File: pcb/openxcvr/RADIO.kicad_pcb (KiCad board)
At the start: 2 copper layers, 99.1 x 63.5 mm, 118 parts, among them J1 UI_CONNECTOR, J2 GPS_CONNECTOR, J3 PA_CONNECTOR, U1 PCM1802, U10 MAX_1000, U11 24LC256, U2 LM386, U3 MCP6002-xSN, U4 FST5253, U5 LM4562, U6 LM4562, U7 LM4562, U8 FST5253, U9 FST5253

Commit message: Get things working with rev 1 PCB
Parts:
- removed C25, C26, C27: 1u, Capacitor_SMD:C_0805_2012Metric
- removed R16, R17: 150, Resistor_SMD:R_0805_2012Metric
- removed R19, R20, R21, R23, R24, R25, R26, R27, R28, R29: 2K2, Resistor_SMD:R_0805_2012Metric
- removed U6, U7: LM4562, Package_SO:SOIC-8_3.9x4.9mm_P1.27mm
- added T1: cx2074NL, openxcvr:bn43-2402-transformer, F.Cu at (122.6, 62.9)
- C20, C21: value 100n -> 22n
- C22, C23: value 100n -> 390p
- C24: value 1u -> 100n
- R12: value 10K -> 1K
- R13: value 10K -> 82
- R14, R15: value 10K -> 100
- U8, U9: value FST5253 -> 74LS251
- moved C24 59.7 mm to (168.2, 98.3)
- moved C31 40.9 mm to (97.8, 63.5)
- moved U11 39.9 mm to (120.7, 95.2)
- moved R30 37.6 mm to (100.3, 58.3), turned to 0 degrees
- moved C23 34.4 mm to (144.8, 78.1)
- moved C36 33.4 mm to (99.1, 97.2), turned to 0 degrees
- moved C49 32.7 mm to (110.5, 69.2), turned to 180 degrees
- moved R12 31.8 mm to (138.4, 83.8), turned to 0 degrees
- moved C32 31.1 mm to (97.8, 102.9)
- moved C21 30.7 mm to (144.8, 70.5), turned to 0 degrees
- moved C40 30.4 mm to (99.1, 94.6), turned to 0 degrees
- moved C45 29.4 mm to (110.5, 71.8), turned to 0 degrees
- moved L5 29.1 mm to (110.5, 76.2), turned to 90 degrees
- moved R15 27.1 mm to (144.8, 73.0)
- moved U9 26.7 mm to (104.1, 63.5), turned to 90 degrees
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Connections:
- C20 pad 1: +2V5 -> GND
- C20 pad 2: I_NEG -> Net-(C20-Pad2)
- C21 pad 1: +2V5 -> GND
- C21 pad 2: Q_NEG -> Net-(C21-Pad2)
- C22 pad 1: I_POS -> Net-(C22-Pad1)
- C22 pad 2: +2V5 -> Net-(C22-Pad2)
- C23 pad 1: Q_POS -> Net-(C23-Pad1)
- C23 pad 2: +2V5 -> Net-(C23-Pad2)
- C24 pad 1: I_POS -> SPEAKER
- C28 pad 1: Net-(C28-Pad1) -> Net-(C22-Pad2)
- C29 pad 1: Net-(C29-Pad1) -> Net-(C23-Pad2)
- R11 pad 1: RF_BPF -> Net-(R11-Pad1)
- R12 pad 1: Net-(C24-Pad2) -> +5V
- R12 pad 2: +2V5 -> Net-(C5-Pad1)
- R13 pad 1: +2V5 -> Net-(R13-Pad1)
- R13 pad 2: Net-(C25-Pad2) -> Net-(R13-Pad2)
- R14 pad 1: Net-(C26-Pad2) -> Net-(C22-Pad1)
- R14 pad 2: +2V5 -> Net-(C20-Pad2)
- R15 pad 1: +2V5 -> Net-(C23-Pad1)
- R15 pad 2: Net-(C27-Pad2) -> Net-(C21-Pad2)
- R18 pad 1: Net-(R16-Pad2) -> Net-(C22-Pad1)
- R18 pad 2: Net-(R18-Pad2) -> Net-(C22-Pad2)
- R2 pad 1: SPEAKER -> Net-(C24-Pad2)
- R22 pad 1: Net-(R18-Pad2) -> Net-(C23-Pad1)
- R22 pad 2: Net-(R22-Pad2) -> Net-(C23-Pad2)
- U4 pad 10: I_POS -> Net-(C21-Pad2)
- U4 pad 11: Q_POS -> Net-(U4-Pad11)
- U4 pad 12: Q_NEG -> Net-(C20-Pad2)
- U4 pad 13: I_NEG -> Net-(U4-Pad13)
- U4 pad 3: I_NEG -> Net-(C21-Pad2)
- U4 pad 4: Q_NEG -> Net-(U4-Pad4)
- U4 pad 5: Q_POS -> Net-(C20-Pad2)
- U4 pad 6: I_POS -> Net-(U4-Pad6)
- U4 pad 9: Net-(R11-Pad2) -> Net-(R13-Pad2)
- U5 pad 1: Net-(R19-Pad2) -> Net-(C23-Pad2)
- U5 pad 2: Net-(R16-Pad1) -> Net-(C23-Pad1)
- U5 pad 3: Net-(C25-Pad2) -> +2V5
- U5 pad 5: Net-(C24-Pad2) -> +2V5
- U5 pad 6: Net-(R16-Pad2) -> Net-(C22-Pad1)
- U5 pad 7: Net-(R18-Pad2) -> Net-(C22-Pad2)
- U8 pad 1: GND -> BPF_2_4_A
- U8 pad 10: BPF_16_30_B -> BAND_1
- U8 pad 11: BPF_8_16_B -> BAND_0
- U8 pad 12: BPF_4_8_B -> Net-(U8-Pad12)
- U8 pad 13: BPF_2_4_B -> Net-(U8-Pad12)
- U8 pad 14: BAND_0 -> Net-(U8-Pad12)
- U8 pad 15: GND -> Net-(U8-Pad12)
- U8 pad 2: BAND_1 -> BPF_4_8_A
- U8 pad 3: BPF_2_4_A -> BPF_8_16_A
- U8 pad 4: BPF_4_8_A -> BPF_16_30_A
- U8 pad 5: BPF_8_16_A -> Net-(C30-Pad2)
- U8 pad 6: BPF_16_30_A -> Net-(U8-Pad6)
- U8 pad 7: BANK_0_A -> GND
- U8 pad 9: BANK_0_B -> BAND_2
- U9 pad 1: GND -> BPF_2_4_B
- U9 pad 10: BANK_0_B -> BAND_1
- U9 pad 11: Net-(U9-Pad11) -> BAND_0
- U9 pad 12: Net-(U9-Pad12) -> Net-(U8-Pad12)
- U9 pad 13: Net-(U9-Pad13) -> Net-(U8-Pad12)
- U9 pad 14: BAND_2 -> Net-(U8-Pad12)
- U9 pad 15: GND -> Net-(U8-Pad12)
- U9 pad 2: GND -> BPF_4_8_B
- U9 pad 3: Net-(U9-Pad3) -> BPF_8_16_B
- U9 pad 4: Net-(U9-Pad4) -> BPF_16_30_B
- U9 pad 5: Net-(U9-Pad11) -> RF_BPF
- U9 pad 6: BANK_0_A -> Net-(U9-Pad6)
- U9 pad 7: Net-(C30-Pad2) -> GND
- U9 pad 9: RF_BPF -> BAND_2
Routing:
- net +5V: track 205.3 -> 283.1 mm, vias 16 -> 8
- net Net-(U8-Pad12): track 0.00 -> 75.6 mm
- net BAND_0: track 27.8 -> 91.5 mm, vias 2 -> 1
- net BAND_1: track 33.5 -> 91.7 mm, vias 2 -> 1
- net GND: track 99.3 -> 44.6 mm, vias 23 -> 58
- net BPF_2_4_B: track 55.9 -> 3.70 mm
- net Net-(C13-Pad1): track 98.1 -> 47.5 mm, vias 0 -> 2
- net Net-(C24-Pad2): track 50.1 -> 3.42 mm
- net BPF_4_8_B: track 46.6 -> 3.64 mm
- net Net-(C26-Pad2): track 42.2 -> 0.00 mm
- net Net-(U10-Pad20): track 45.6 -> 5.41 mm, vias 2 -> 0
- net BAND_2: track 28.0 -> 64.3 mm, vias 2 -> 1
- net +2V5: track 147.6 -> 183.8 mm, vias 8 -> 2
- net I_POS: track 35.2 -> 0.00 mm
- net LCD_CONTRAST: track 36.0 -> 70.8 mm
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
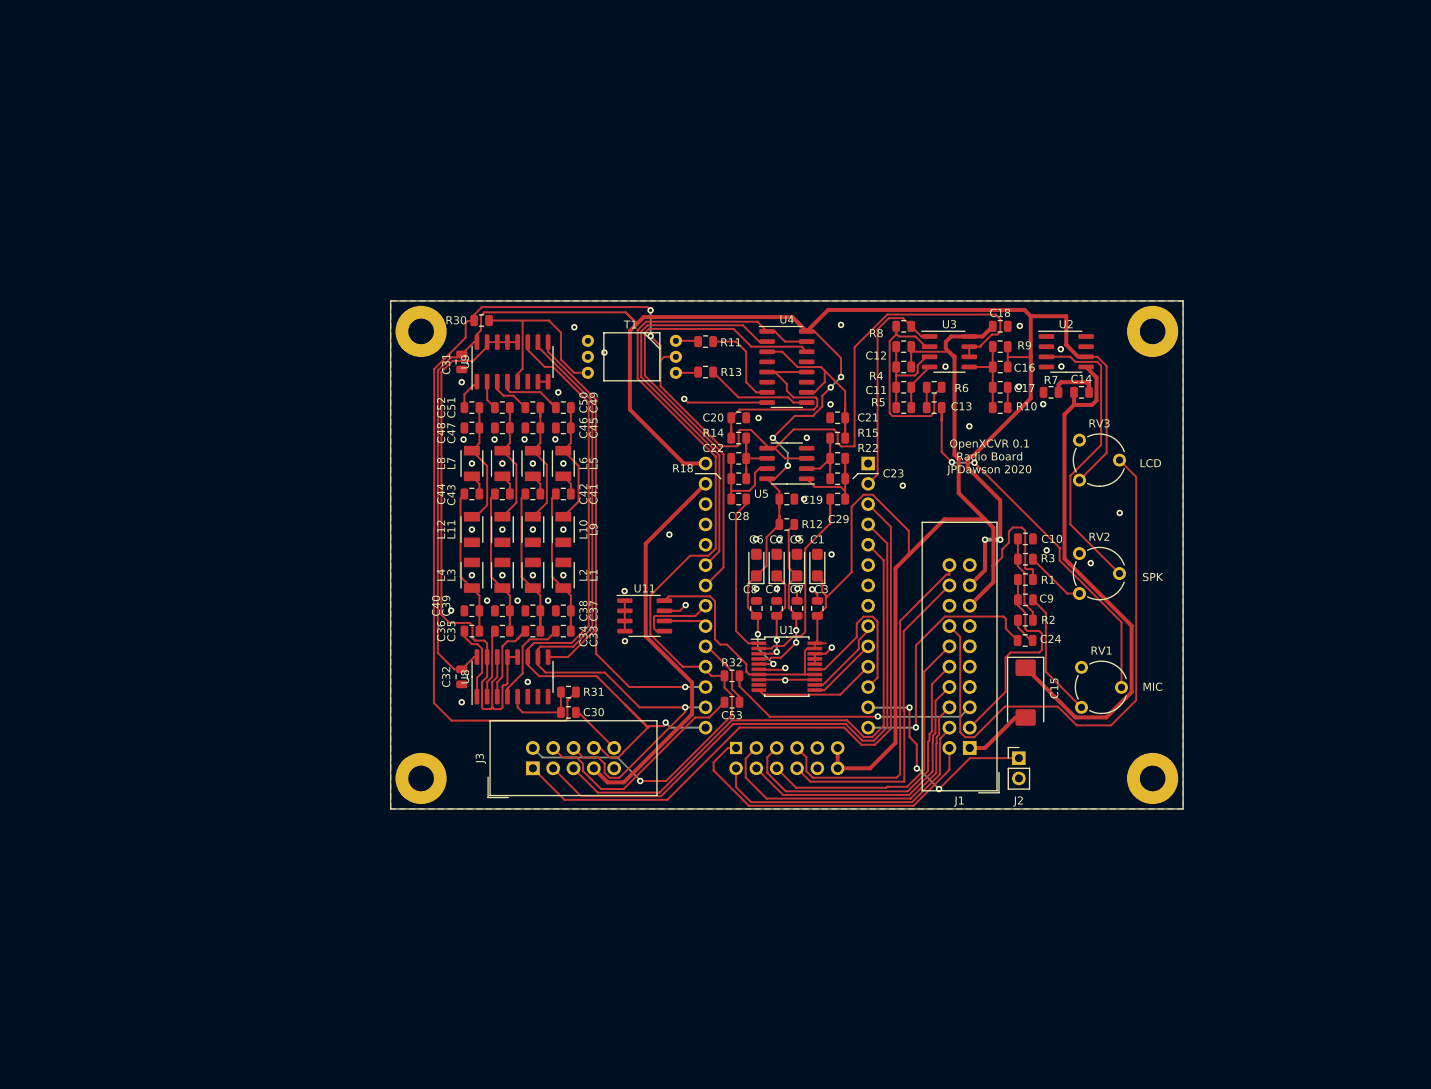
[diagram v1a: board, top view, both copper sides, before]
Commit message: Add eeprom load store capability
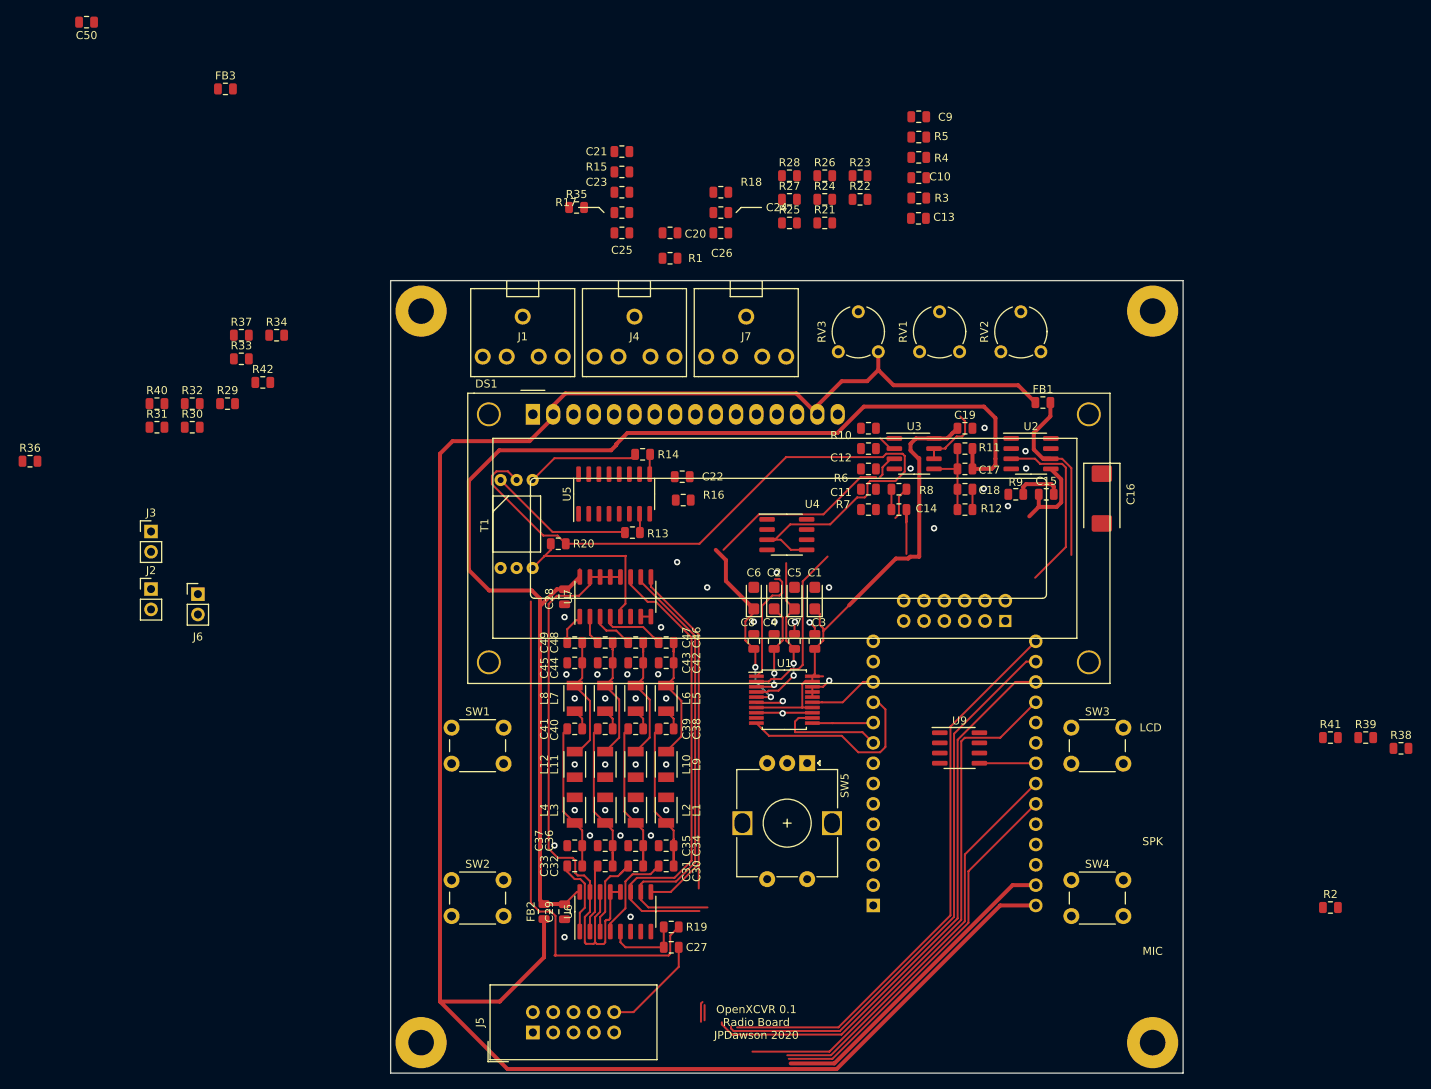
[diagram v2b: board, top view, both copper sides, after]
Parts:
- added DS1: WC1602A, Display:WC1602A, F.Cu at (106.7, 70.1)
- added FB1: Ferrite_Bead, Inductor_SMD:L_0805_2012Metric, F.Cu at (170.4, 68.6)
- added FB2: Ferrite_Bead, Inductor_SMD:L_0805_2012Metric, F.Cu at (108.1, 132.2)
- added FB3: Ferrite_Bead, Inductor_SMD:L_0805_2012Metric, F.Cu at (68.3, 29.4)
- added J2: Mic, Connector_PinHeader_2.54mm:PinHeader_1x02_P2.54mm_Vertical, F.Cu at (59.0, 91.9)
- added J3: Speaker, Connector_PinHeader_2.54mm:PinHeader_1x02_P2.54mm_Vertical, F.Cu at (59.0, 84.7)
- added J4: Headphone, openxcvr:jack3.5mm switched, F.Cu at (119.4, 53.3)
- added J7: PTT, openxcvr:jack3.5mm switched, F.Cu at (133.3, 53.3)
- added R2: 1K, Resistor_SMD:R_0805_2012Metric, F.Cu at (206.4, 131.7)
- added R21: 100, Resistor_SMD:R_0805_2012Metric, F.Cu at (143.2, 46.1)
- added R22: 100, Resistor_SMD:R_0805_2012Metric, F.Cu at (147.6, 43.2)
- added R23: 100, Resistor_SMD:R_0805_2012Metric, F.Cu at (147.6, 40.2)
- added R24: 100, Resistor_SMD:R_0805_2012Metric, F.Cu at (143.2, 43.2)
- added R25: 100, Resistor_SMD:R_0805_2012Metric, F.Cu at (138.8, 46.1)
- added R26: 100, Resistor_SMD:R_0805_2012Metric, F.Cu at (143.2, 40.2)
- added R27: 100, Resistor_SMD:R_0805_2012Metric, F.Cu at (138.8, 43.2)
- added R28: 100, Resistor_SMD:R_0805_2012Metric, F.Cu at (138.8, 40.2)
- added R29: 10K, Resistor_SMD:R_0805_2012Metric, F.Cu at (68.5, 68.7)
- added R30: 10K, Resistor_SMD:R_0805_2012Metric, F.Cu at (64.1, 71.7)
- added R31: 10K, Resistor_SMD:R_0805_2012Metric, F.Cu at (59.7, 71.7)
- added R33: 10K, Resistor_SMD:R_0805_2012Metric, F.Cu at (70.2, 63.1)
- added R34: 2K2, Resistor_SMD:R_0805_2012Metric, F.Cu at (74.7, 60.2)
- added R35: 2K2, Resistor_SMD:R_0805_2012Metric, F.Cu at (112.1, 44.2)
- added R36: 2K2, Resistor_SMD:R_0805_2012Metric, F.Cu at (43.8, 75.9)
- added R37: 2K2, Resistor_SMD:R_0805_2012Metric, F.Cu at (70.2, 60.2)
- added R38: 2K2, Resistor_SMD:R_0805_2012Metric, F.Cu at (215.2, 111.8)
- added R39: 2K2, Resistor_SMD:R_0805_2012Metric, F.Cu at (210.8, 110.5)
- added R40: 10K, Resistor_SMD:R_0805_2012Metric, F.Cu at (59.7, 68.7)
- added R41: 2K2, Resistor_SMD:R_0805_2012Metric, F.Cu at (206.4, 110.5)
- added R42: 10K, Resistor_SMD:R_0805_2012Metric, F.Cu at (72.9, 66.1)
- added SW1: SW_Push, Button_Switch_THT:SW_PUSH_6mm, F.Cu at (96.5, 109.2)
- added SW2: SW_Push, Button_Switch_THT:SW_PUSH_6mm, F.Cu at (96.5, 128.3)
- added SW3: SW_Push, Button_Switch_THT:SW_PUSH_6mm, F.Cu at (174.0, 109.2)
- added SW4: SW_Push, Button_Switch_THT:SW_PUSH_6mm, F.Cu at (174.0, 128.3)
- added SW5: Rotary_Encoder_Switch, Rotary_Encoder:RotaryEncoder_Alps_EC12E-Switch_Vertical_H20mm, F.Cu at (141.0, 113.7)
- C23: renamed from C22; value 390p -> 1n
- C24: renamed from C23; value 390p -> 1n
- J1: value UI_CONNECTOR -> Microphone; footprint Connector_IDC:IDC-Header_2x10_P2.54mm_Vertical -> openxcvr:jack3.5mm switched
- T1: value cx2074NL -> BN43-24023
- moved C50 117.2 mm to (50.9, 21.0)
- moved J6 104.7 mm to (64.8, 92.5)
- moved U8 103.1 mm to (159.4, 154.3), turned to 0 degrees
- moved J1 80.8 mm to (105.4, 53.3), turned to 0 degrees
- moved R32 75.6 mm to (64.1, 68.7)
- moved C13 54.4 mm to (154.9, 45.6)
- moved R5 54.4 mm to (154.9, 35.4)
- moved C10 54.4 mm to (154.9, 40.5)
- moved C9 54.4 mm to (154.9, 32.9)
- moved R4 54.4 mm to (154.9, 37.9)
- moved R3 54.4 mm to (154.9, 43.0)
- moved RV2 44.7 mm to (170.2, 62.2), turned to 90 degrees
- moved U9 42.7 mm to (160.0, 111.8)
- moved R15 36.3 mm to (117.8, 39.8)
- moved C21 36.3 mm to (117.8, 37.2)
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- renumbered C9 to C10, C24 to C13, C13 to C14, C14 to C15, C15 to C16, C16 to C17, C17 to C18, C18 to C19, C19 to C20, C20 to C21, C21 to C22, C28 to C25, C29 to C26, C30 to C27, C31 to C28, C32 to C29, C33 to C30, C34 to C31, C35 to C32, C36 to C33, C37 to C34, C38 to C35, C39 to C36, C40 to C37, C41 to C38, C42 to C39, C43 to C40, C44 to C41, C45 to C42, C46 to C43, C47 to C44, C48 to C45, C49 to C46, C50 to C47, C51 to C48, C52 to C49, C53 to C50, C10 to C9, J3 to J5, J2 to J6, R12 to R1, R8 to R10, R9 to R11, R10 to R12, R11 to R13, R13 to R14, R14 to R15, R15 to R16, R18 to R17, R22 to R18, R31 to R19, R30 to R20, R2 to R3, R1 to R4, R3 to R5, R4 to R6, R5 to R7, R6 to R8, R7 to R9, RV2 to RV1, RV1 to RV2, U5 to U4, U4 to U5, U8 to U6, U9 to U7, U10 to U8, U11 to U9
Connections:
- C10 pad 1: MIC_HDR -> Net-(C10-Pad1)
- C13 pad 1: SPEAKER -> Net-(C13-Pad1)
- C13 pad 2: Net-(C24-Pad2) (its old number) -> Net-(C13-Pad2)
- C16 pad 2: SPEAKER_HDR -> Net-(C16-Pad2)
- C21 pad 2: Net-(C20-Pad2) -> Net-(C21-Pad2)
- R15 pad 2: Net-(C20-Pad2) -> Net-(C21-Pad2)
- R3 pad 1: Net-(C24-Pad2) (its old number) -> SPEAKER
- R32 pad 1: TX_ENABLE -> LCD7
- R32 pad 2: Net-(J1-Pad5) -> Net-(R32-Pad2)
- R4 pad 2: MIC_HDR -> Net-(C10-Pad1)
- RV1 pad 2: Net-(RV2-Pad2) -> Net-(C13-Pad1)
- RV3 pad 1: +5V -> +5VD
- RV3 pad 2: LCD_CONTRAST -> Net-(DS1-Pad3)
- U2 pad 3: Net-(RV2-Pad2) -> Net-(C13-Pad2)
- U2 pad 6: +5V -> +5VA
- U5 pad 12: Net-(C20-Pad2) -> Net-(U5-Pad12)
- U5 pad 13: Net-(U4-Pad13) -> Net-(C21-Pad2)
- U5 pad 5: Net-(C20-Pad2) -> Net-(U5-Pad5)
- U5 pad 6: Net-(U4-Pad6) -> Net-(C21-Pad2)
- U8 pad 28: +5V -> +5VD
- U8 pad 29: LCD7 -> Net-(R21-Pad2)
- U8 pad 30: LCD5 -> Net-(R22-Pad2)
- U8 pad 31: LCD_RS -> Net-(R23-Pad2)
- U8 pad 32: PB_1 -> Net-(R24-Pad2)
- U8 pad 34: +3V3 -> Net-(FB3-Pad1)
- U8 pad 35: LCD6 -> Net-(R25-Pad1)
- U8 pad 36: LCD4 -> Net-(R26-Pad1)
- U8 pad 37: LCD_E -> Net-(R27-Pad1)
- U8 pad 38: PB_0 -> Net-(R28-Pad1)
- U8 pad 40: +3V3 -> Net-(FB3-Pad1)
- U8 pad 6: Net-(U10-Pad6) -> PTT
- U8 pad 7: Net-(U10-Pad7) -> DIT
- U8 pad 8: Net-(U10-Pad8) -> DAH
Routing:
- net +5VD: track 0.00 -> 261.4 mm
- net +3V3: track 181.7 -> 60.6 mm
- net BATTERY: track 81.1 -> 0.00 mm
- net +5V: track 283.1 -> 202.1 mm, vias 8 -> 2
- net FWD_PWR: track 74.9 -> 0.00 mm
- net LCD_CONTRAST: track 70.8 -> 0.00 mm
- net REV_PWR: track 68.7 -> 0.00 mm
- net BAND_2: track 64.3 -> 120.2 mm, vias 1 -> 0
- net Net-(C15-Pad1): track 66.3 -> 11.0 mm
- net TX_ENABLE: track 116.6 -> 66.6 mm, vias 1 -> 0
- net PB_1: track 44.5 -> 0.00 mm
- net PB_0: track 41.0 -> 0.00 mm
- net LCD7: track 40.5 -> 0.00 mm
- net Net-(C14-Pad1): track 47.5 -> 7.17 mm, vias 2 -> 0
- net LCD_RS: track 39.9 -> 0.00 mm
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- removed copper zone on B.Cu, net GND
- removed copper zone on F.Cu, net GND
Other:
- board size 99.1 x 63.5 mm -> 99.1 x 99.1 mm

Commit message: update rev0.2 PCB
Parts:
- removed C16: 100u, Capacitor_Tantalum_SMD:CP_EIA-7343-31_Kemet-D
- removed C50: 100n, Capacitor_SMD:C_0805_2012Metric
- removed RV1, RV2: 10K, Potentiometer_THT:Potentiometer_Piher_PT-6-V_Vertical
- added C51: 100n, Capacitor_SMD:C_0805_2012Metric, B.Cu at (172.6, 139.6)
- added J8: Conn_01x03_Male, Connector_PinHeader_2.54mm:PinHeader_1x03_P2.54mm_Vertical, F.Cu at (180.6, 116.8)
- C1, C10, C11, C12, C13, C14, C17, C18, C19, C2, C20, C21, C22, C23, C24, C25, C26, C27, C28, C29, C3, C30, C31, C32, C33, C34, C35, C36, C37, C38, C39, C4, C40, C41, C42, C43, C44, C45, C46, C47, C48, C49, C5, C6, C7, C8, C9, FB1, FB2, FB3, L1, L10, L11, L12, L2, L3, L4, L5, L6, L7, L8, L9, R1, R10, R11, R12, R13, R14, R15, R16, R17, R18, R19, R2, R20, R21, R22, R23, R24, R25, R26, R27, R28, R29, R3, R30, R31, R32, R33, R34, R35, R36, R37, R38, R39, R4, R40, R41, R42, R5, R6, R7, R8, T1, U1, U3, U4, U5, U6, U7, U9: moved to B.Cu
- C15: value 47n -> 100n; moved to B.Cu
- J5: value PA_CONNECTOR -> Conn_02x08_Odd_Even; footprint Connector_IDC:IDC-Header_2x05_P2.54mm_Vertical -> Connector_PinHeader_2.54mm:PinHeader_2x08_P2.54mm_Vertical
- R9: value 10 -> 50k; moved to B.Cu
- U2: value LM386 -> TPA711; moved to B.Cu
- moved FB3 133.5 mm to (168.5, 117.5), turned to -90 degrees
- moved R40 121.2 mm to (170.7, 117.5), turned to -90 degrees
- moved C21 118.7 mm to (181.0, 137.7), turned to 0 degrees
- moved R15 114.7 mm to (181.0, 135.5)
- moved J6 112.5 mm to (175.5, 112.6), turned to 90 degrees
- moved R42 112.4 mm to (172.8, 117.5), turned to -90 degrees
- moved C23 109.0 mm to (180.9, 131.2)
- moved R17 108.7 mm to (181.0, 133.3)
- moved C20 104.1 mm to (177.2, 136.8), turned to 180 degrees
- moved C25 103.2 mm to (181.0, 129.0)
- moved U8 101.5 mm to (160.7, 52.8), turned to 180 degrees
- moved R18 98.7 mm to (169.4, 132.8)
- moved C24 94.4 mm to (169.4, 130.7)
- moved R36 91.6 mm to (132.2, 100.1)
- moved C26 90.1 mm to (169.4, 128.5)
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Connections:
- C10 pad 1: Net-(C10-Pad1) -> GND
- C15 pad 1: Net-(C15-Pad1) -> GND
- C15 pad 2: Net-(C15-Pad2) -> +5VA
- C9 pad 1: Net-(C9-Pad1) -> Net-(C13-Pad1)
- J1 pad T: Net-(C10-Pad1) -> Net-(C14-Pad1)
- J3 pad 2: GND -> Net-(J3-Pad2)
- J4 pad S: Net-(C16-Pad2) -> Net-(J4-PadS)
- J4 pad SN: Net-(J4-PadSN) -> Net-(J3-Pad1)
- J4 pad T: Net-(C16-Pad2) -> Net-(J4-PadT)
- J4 pad TN: Net-(J3-Pad1) -> Net-(J3-Pad2)
- J5 pad 4: RF_OUT -> BAND_2
- J5 pad 9: GND -> RF_OUT
- R3 pad 2: Net-(C9-Pad1) -> Net-(C13-Pad1)
- R4 pad 2: Net-(C10-Pad1) -> Net-(C14-Pad1)
- R5 pad 1: Net-(C9-Pad1) -> Net-(C13-Pad2)
- R9 pad 1: Net-(C15-Pad2) -> Net-(R5-Pad2)
- R9 pad 2: GND -> Net-(J4-PadT)
- U2 pad 1: Net-(U2-Pad1) -> GND
- U2 pad 2: GND -> Net-(C10-Pad2)
- U2 pad 3: Net-(C13-Pad2) -> GND
- U2 pad 4: GND -> Net-(R5-Pad2)
- U2 pad 5: Net-(C15-Pad1) -> Net-(J4-PadT)
- U2 pad 7: Net-(U2-Pad7) -> GND
- U2 pad 8: Net-(U2-Pad8) -> Net-(J4-PadS)
- U8 pad 19: Net-(C50-Pad1) -> RF_OUT
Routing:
- net +3V3: track 60.6 -> 217.8 mm, vias 0 -> 16
- net +5VD: track 261.4 -> 127.2 mm
- net 5V_IN: track 39.9 -> 171.4 mm, vias 0 -> 1
- net Net-(C13-Pad1): track 0.00 -> 123.9 mm, vias 0 -> 2
- net REV_PWR: track 0.00 -> 119.9 mm, vias 0 -> 2
- net FWD_PWR: track 0.00 -> 119.0 mm, vias 0 -> 2
- net BATTERY: track 0.00 -> 116.4 mm, vias 0 -> 2
- net LCD_RS: track 0.00 -> 115.7 mm, vias 0 -> 2
- net LO_Q: track 50.4 -> 157.8 mm, vias 0 -> 3
- net LCD_E: track 0.00 -> 106.9 mm, vias 0 -> 2
- net LO_I: track 51.9 -> 156.5 mm, vias 0 -> 4
- net +5V: track 202.1 -> 291.8 mm, vias 2 -> 10
- net RF_OUT: track 0.00 -> 87.4 mm, vias 0 -> 2
- net PTT: track 0.00 -> 83.0 mm, vias 0 -> 2
- net LCD4: track 0.00 -> 81.6 mm, vias 0 -> 2
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- added copper zone on B.Cu, net GND
- added copper zone on F.Cu, net GND
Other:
- board text added: "Audio ADC"
- board text added: "Audio Amplifier"
- board text added: "Band Pass Filter"
- board text added: "EEPROM"
- board text added: "KEY"
- board text added: "LCD Contrast"
- board text added: "Micorphone Pre Amplifier"
- board text added: "Microphone"
- board text added: "OpenXCVR 0.2 Radio Board JPDawson 2020"
- board text added: "PHONES"
- board text added: "Quadrature Sampling Detector"
- board text added: "Speaker"
- board text removed: "LCD"
- board text removed: "OpenXCVR 0.1 Radio Board JPDawson 2020"
- board text removed: "SPK"

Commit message: Review and update schematic
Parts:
- added C16: 100n, Capacitor_SMD:C_0805_2012Metric, B.Cu at (174.6, 68.6)
- added C50: 47p, Capacitor_SMD:C_0805_2012Metric, B.Cu at (111.0, 98.0)
- added R43: 0, Resistor_SMD:R_0805_2012Metric, B.Cu at (144.8, 67.6)
- added R44: 0, Resistor_SMD:R_0805_2012Metric, B.Cu at (144.8, 71.1)
- R9: value 50k -> 47k
- T1: value BN43-24023 -> BN43-2402
- U2: value TPA711 -> TPA711D
- U5: value FST5253 -> FST3253
- U6, U7: value 74LS251 -> 74CBT3251
- moved C19 64.2 mm to (118.7, 100.2), turned to 0 degrees
- moved FB2 11.2 mm to (96.5, 76.2), turned to 0 degrees
- moved C11 2.16 mm to (111.0, 100.2)
- moved C12 2.16 mm to (114.8, 100.2)
- moved R6 2.16 mm to (114.8, 102.4)
- moved R7 2.16 mm to (111.0, 102.4)
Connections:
- U5 pad 10: Net-(C22-Pad2) -> Net-(U5-Pad10)
- U5 pad 12: Net-(U5-Pad12) -> Net-(C22-Pad2)
- U5 pad 3: Net-(C22-Pad2) -> Net-(U5-Pad3)
- U5 pad 5: Net-(U5-Pad5) -> Net-(C22-Pad2)
- U8 pad 28: +5VD -> Net-(R43-Pad1)
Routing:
- net +5VD: track 127.2 -> 108.0 mm
- net Net-(R43-Pad1): track 0.00 -> 11.2 mm
- net 5V_IN: track 171.4 -> 180.6 mm
- net +5V: track 291.8 -> 286.1 mm
- net +3V3: track 217.8 -> 222.2 mm
- net +2V5: track 215.2 -> 211.8 mm
- net MIC: track 81.3 -> 83.5 mm
- net Net-(C50-Pad1): track 5.55 -> 7.71 mm
- net Net-(J4-PadT): track 43.1 -> 41.1 mm
- net Net-(C11-Pad1): track 18.4 -> 19.9 mm
- net Net-(J3-Pad1): track 14.3 -> 12.9 mm
- net PTT: track 83.0 -> 81.7 mm
- net +5VA: track 7.61 -> 8.37 mm
- net Net-(C22-Pad2): track 34.3 -> 34.8 mm
- net Net-(J3-Pad2): track 22.9 -> 22.3 mm
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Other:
- board text added: "EXTERNAL POWER"
- board text added: "GPS/TEST"
- board text added: "I_Q_TEST"
- board text added: "USB POWER"
